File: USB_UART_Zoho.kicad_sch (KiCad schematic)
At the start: 25 parts, among them J1 USB_C_Receptacle, J2 Peripherals, J3 Cbus, J4 VccIo_jumper, J5 POWER, U1 FT232RL, U2 USBLC6-2P6

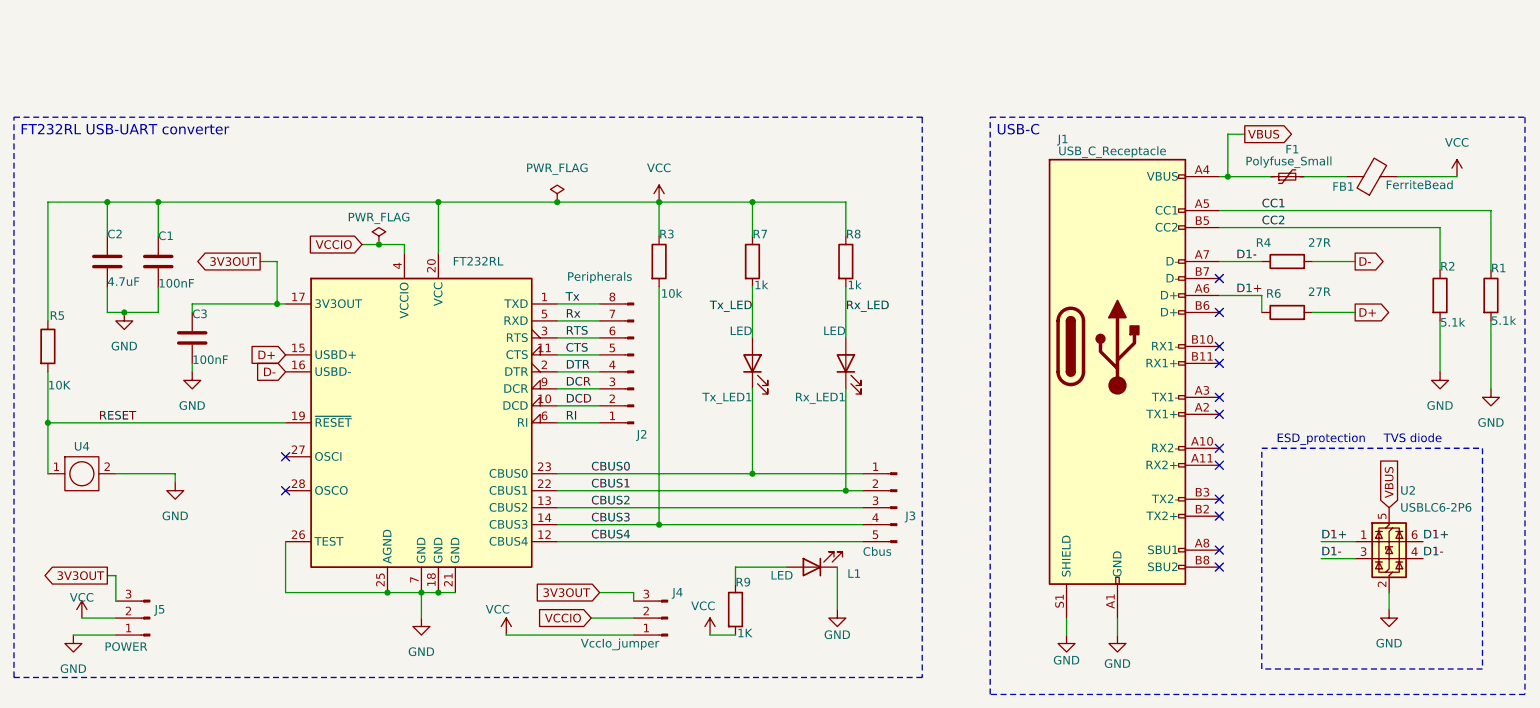
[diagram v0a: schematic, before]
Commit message: improved design decisions from the previous layout
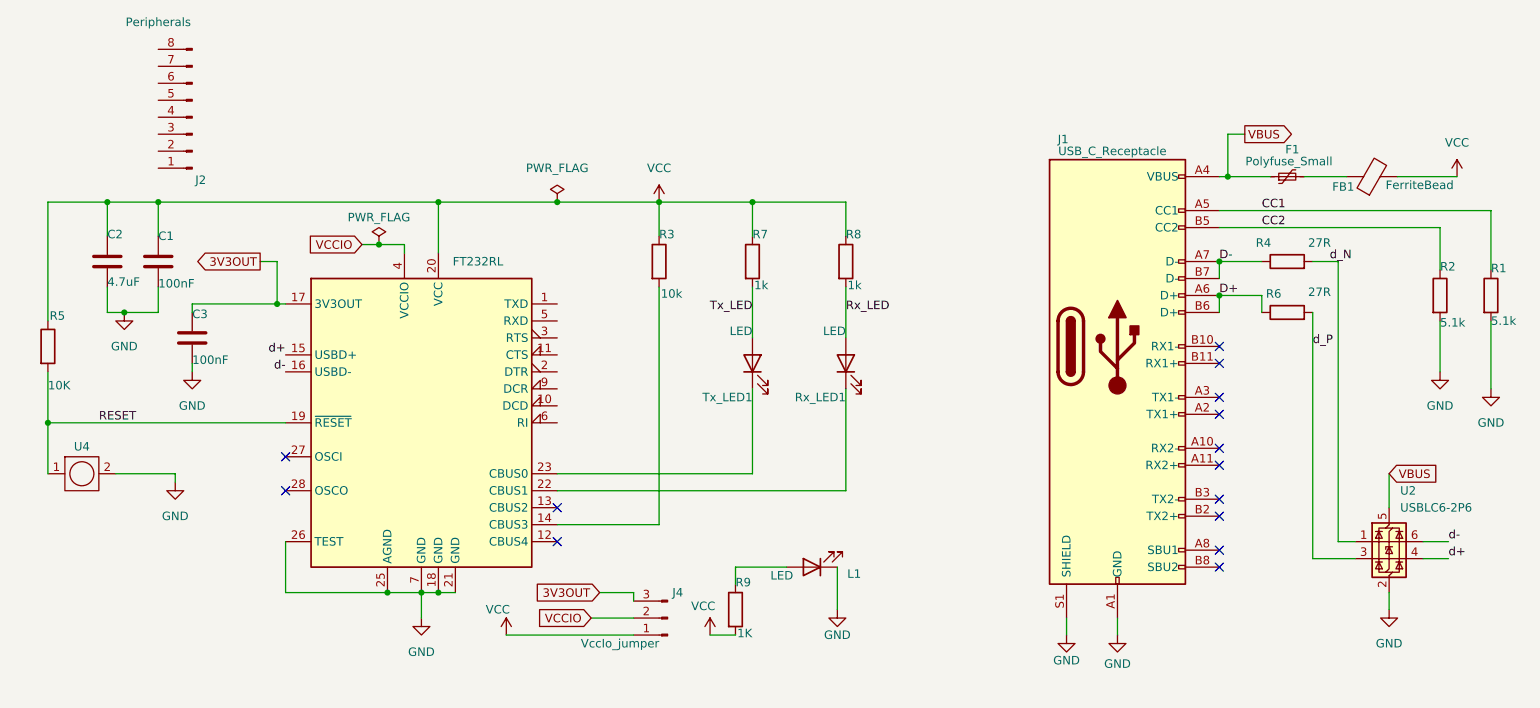
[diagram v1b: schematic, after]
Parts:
- removed J3: Cbus, Connector_PinHeader_2.54mm:PinHeader_1x05_P2.54mm_Vertical, symbol Connector:Conn_01x05_Pin
- removed J5: POWER, Connector_PinHeader_2.54mm:PinHeader_1x03_P2.54mm_Vertical, symbol Connector:Conn_01x03_Pin
- U4: value ~ -> (none)
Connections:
- net D+: now also J1.A6 (D+), J1.B6 (D+), R6.1; no longer R6.2, U1.15 (USBD+)
- net D-: now also J1.A7 (D-), J1.B7 (D-), R4.1; no longer R4.2, U1.16 (USBD-)
- net CBUS0: no longer names the net of Tx_LED1.1 (K), U1.23 (CBUS0)
- net CBUS1: no longer names the net of Rx_LED1.1 (K), U1.22 (CBUS1)
- net CBUS2: no longer names the net of U1.13 (CBUS2)
- net CBUS3: no longer names the net of R3.2, U1.14 (CBUS3)
- net CBUS4: no longer names the net of U1.12 (CBUS4)
- net CTS: no longer names the net of U1.11 (CTS)
- net CTS: no longer J2.5 (Pin_5)
- removed net D1+: J1.A6 (D+), R6.1, U2.1 (I/O1), U2.6 (I/O1)
- removed net D1-: J1.A7 (D-), R4.1, U2.3 (I/O2), U2.4 (I/O2)
- net DCD: no longer names the net of U1.10 (DCD)
- net DCD: no longer J2.2 (Pin_2)
- net DCR: no longer names the net of U1.9 (DCR)
- net DCR: no longer J2.3 (Pin_3)
- net DTR: no longer names the net of U1.2 (DTR)
- net DTR: no longer J2.4 (Pin_4)
- net RI: no longer names the net of U1.6 (RI)
- net RI: no longer J2.1 (Pin_1)
- net RTS: no longer names the net of U1.3 (RTS)
- net RTS: no longer J2.6 (Pin_6)
- net Rx: no longer names the net of U1.5 (RXD)
- net Rx: no longer J2.7 (Pin_7)
- net Tx: no longer names the net of U1.1 (TXD)
- net Tx: no longer J2.8 (Pin_8)
- new net d+: U1.15 (USBD+), U2.4 (I/O2)
- new net d-: U1.16 (USBD-), U2.6 (I/O1)
- new net d_N: R4.2, U2.1 (I/O1)
- new net d_P: R6.2, U2.3 (I/O2)
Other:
- note removed: "ESD_protection"
- note removed: "TVS diode"
- moved on the sheet: J2
